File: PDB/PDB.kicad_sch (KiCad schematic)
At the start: 0 parts

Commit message: test
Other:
- added sheet 5V@12A (5v.kicad_sch)
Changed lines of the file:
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@@
 	(generator "eeschema")
 	(generator_version "9.0")
-	(paper "A4")
+	(paper "User" 424.18 177.8)
+	(sheet
+		(at 125.73 40.64)
+		(size 25.4 8.89)
+		(exclude_from_sim no)
+		(in_bom yes)
+		(on_board yes)
+		(dnp no)
+		(fields_autoplaced yes)
+		(stroke
+			(width 0.1524)
+			(type solid)
+		)
+		(fill
+			(color 0 0 0 0.0000)
+		)
+		(property "Sheetname" "5V@12A"
+			(at 125.73 39.9284 0)
+			(effects
+				(font
+					(size 1.27 1.27)
+				)
+				(justify left bottom)
+			)
+		)
+		(property "Sheetfile" "5v.kicad_sch"
+			(at 125.73 50.1146 0)
+			(effects
+				(font
+					(size 1.27 1.27)
+				)
+				(justify left top)
+			)
+		)
+		(instances
+			(project "PDB"
+				(path "/a9cf05c4-aac5-4cf1-b700-1d3045f8dfbd"
+					(page "2")
+				)
+			)
+		)
+	)
 	(sheet_instances
 		(path "/"

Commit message: did the microcontroller
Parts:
- added C10, C13: 2.2uF, Capacitor_SMD:C_1206_3216Metric, symbol Device:C
- added C11, C17, C19, C20, C21, C9: 100nF, Capacitor_SMD:C_1206_3216Metric, symbol Device:C
- added C8: 4.7uF, Capacitor_SMD:C_1206_3216Metric, symbol Device:C
- added D3, D4, D5, D6, D7: LED, LED_SMD:LED_0805_2012Metric, symbol Device:LED
- added R16, R27, R6, R8, R9: 270, Resistor_SMD:R_1206_3216Metric_Pad1.30x1.75mm_HandSolder, symbol Device:R
- added TP5, TP6: TestPoint, TestPoint:TestPoint_Pad_D2.5mm, symbol Connector:TestPoint
- added U2: STM32H742VGTx, Package_QFP:LQFP-100_14x14mm_P0.5mm, symbol MCU_ST_STM32H7:STM32H742VGTx
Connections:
- new net: R27.1, U2.52 (PB13)
- new net: D7.2 (A), R27.2
- new net: C13.2, U2.48 (VCAP)
- new net: R8.1, U2.45 (PE15)
- new net: D4.2 (A), R8.2
- new net: R16.1, U2.51 (PB12)
- new net: D6.2 (A), R16.2
- new net: R9.1, U2.44 (PE14)
- new net: D5.2 (A), R9.2
- new net: R6.1, U2.43 (PE13)
- new net: C10.2, U2.73 (VCAP)
- new net: D3.2 (A), R6.2
- new net +3.3V: C11.2, C17.1, C19.1, C20.1, C21.1, C8.1, C9.1, TP6.1, U2.100 (VDD), U2.11 (VDD), U2.20 (VREF+), U2.21 (VDDA), U2.27 (VDD), U2.50 (VDD), U2.75 (VDD)
- new net BOOT0: U2.94 (BOOT0)
- new net CS: U2.28 (PA4)
- new net D+: U2.71 (PA12)
- new net D-: U2.70 (PA11)
- new net GND: C10.1, C11.1, C13.1, C17.2, C19.2, C20.2, C21.2, C8.2, C9.2, D3.1 (K), D4.1 (K), D5.1 (K), D6.1 (K), D7.1 (K), TP5.1, U2.10 (VSS), U2.19 (VSSA), U2.26 (VSS), U2.49 (VSS), U2.74 (VSS), U2.99 (VSS)
- new net INT: U2.67 (PA8)
- new net MISO: U2.30 (PA6)
- new net MOSI: U2.31 (PA7)
- new net PA0: U2.22 (PA0)
- new net PA3: U2.25 (PA3)
- new net PB0: U2.34 (PB0)
- new net PB1: U2.35 (PB1)
- new net PB10: U2.46 (PB10)
- new net PB11: U2.47 (PB11)
- new net PB2: U2.36 (PB2)
- new net PC0: U2.15 (PC0)
- new net PC2: U2.17 (PC2_C)
- new net PC3: U2.18 (PC3_C)
- new net PC4: U2.32 (PC4)
- new net PC5: U2.33 (PC5)
- new net PE11: U2.41 (PE11)
- new net PE12: U2.42 (PE12)
- new net PE7: U2.37 (PE7)
- new net PE8: U2.38 (PE8)
- new net PE9: U2.39 (PE9)
- new net RST: U2.68 (PA9)
- new net SCK: U2.29 (PA5)
- new net SWCLK: U2.76 (PA14)
- new net SWDIO: U2.72 (PA13)
- new net SWO/TRACE: U2.89 (PB3)
- no-connect marks 0 -> 51
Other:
- note added: "TBD"

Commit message: Add 5V@4A
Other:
- added sheet 3V3@1A (3v3_1a.kicad_sch)
- added sheet 5V@4A (5v_4a.kicad_sch)
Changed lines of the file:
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@@
+		)
+	)
+	(sheet
+		(at 271.78 52.07)
+		(size 17.78 8.89)
+		(exclude_from_sim no)
+		(in_bom yes)
+		(on_board yes)
+		(dnp no)
+		(fields_autoplaced yes)
+		(stroke
+			(width 0.1524)
+			(type solid)
+		)
+		(fill
+			(color 0 0 0 0)
+		)
+		(property "Sheetname" "3V3@1A"
+			(at 271.78 51.3584 0)
+			(show_name no)
+			(do_not_autoplace no)
+			(effects
+				(font
+					(size 1.27 1.27)
+				)
+				(justify left bottom)
+			)
+		)
+		(property "Sheetfile" "3v3_1a.kicad_sch"
+			(at 271.78 61.5446 0)
+			(show_name no)
+			(do_not_autoplace no)
+			(effects
+				(font
+					(size 1.27 1.27)
+				)
+				(justify left top)
+			)
+		)
+		(instances
+			(project "PDB"
+				(path "/a9cf05c4-aac5-4cf1-b700-1d3045f8dfbd"
+					(page "4")
+				)
+			)
+		)
+	)
+	(sheet
+		(at 271.78 38.1)
+		(size 17.78 8.89)
+		(exclude_from_sim no)
+		(in_bom yes)
+		(on_board yes)
+		(dnp no)
+		(fields_autoplaced yes)
+		(stroke
+			(width 0.1524)
+			(type solid)
+		)
+		(fill
+			(color 0 0 0 0)
+		)
+		(property "Sheetname" "5V@4A"
+			(at 271.78 37.3884 0)
+			(show_name no)
+			(do_not_autoplace no)
+			(effects
+				(font
+					(size 1.27 1.27)
+				)
+				(justify left bottom)
+			)
+		)
+		(property "Sheetfile" "5v_4a.kicad_sch"
+			(at 271.78 47.5746 0)
+			(show_name no)
+			(do_not_autoplace no)
+			(effects
+				(font
+					(size 1.27 1.27)
+				)
+				(justify left top)
+			)
+		)
+		(instances
+			(project "PDB"
+				(path "/a9cf05c4-aac5-4cf1-b700-1d3045f8dfbd"
+					(page "3")
+				)
+			)
 		)
 	)

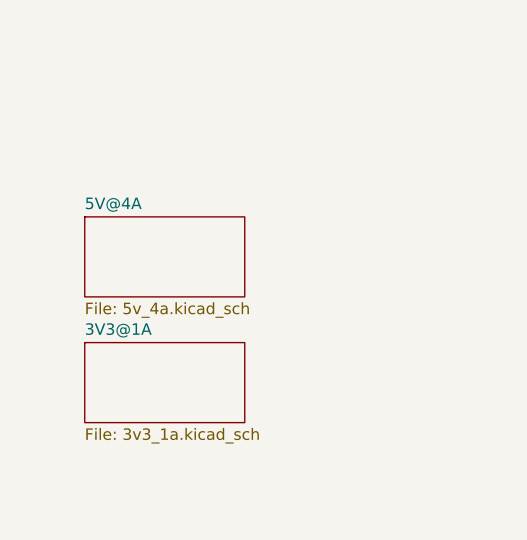
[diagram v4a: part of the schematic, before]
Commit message: Add 3v3@1a
unified the batery lables between sub schematics and changed Iout symbols for power pins to avoid layout issues for trying to match multiple bateries and Iouts without footprints
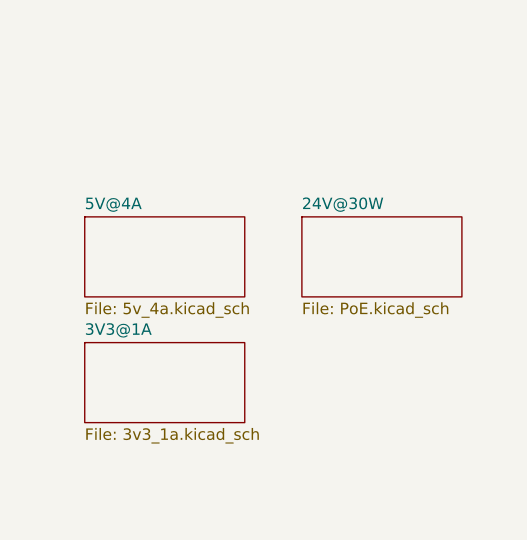
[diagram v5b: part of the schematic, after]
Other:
- added sheet 24V@30W (PoE.kicad_sch)
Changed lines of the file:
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@@
+	)
+	(sheet
+		(at 295.91 38.1)
+		(size 17.78 8.89)
+		(exclude_from_sim no)
+		(in_bom yes)
+		(on_board yes)
+		(dnp no)
+		(fields_autoplaced yes)
+		(stroke
+			(width 0.1524)
+			(type solid)
+		)
+		(fill
+			(color 0 0 0 0)
+		)
+		(property "Sheetname" "24V@30W"
+			(at 295.91 37.3884 0)
+			(show_name no)
+			(do_not_autoplace no)
+			(effects
+				(font
+					(size 1.27 1.27)
+				)
+				(justify left bottom)
+			)
+		)
+		(property "Sheetfile" "PoE.kicad_sch"
+			(at 295.91 47.5746 0)
+			(show_name no)
+			(do_not_autoplace no)
+			(effects
+				(font
+					(size 1.27 1.27)
+				)
+				(justify left top)
+			)
+		)
+		(instances
+			(project "PDB"
+				(path "/a9cf05c4-aac5-4cf1-b700-1d3045f8dfbd"
+					(page "5")
+				)
+			)
+		)
 	)
 	(sheet

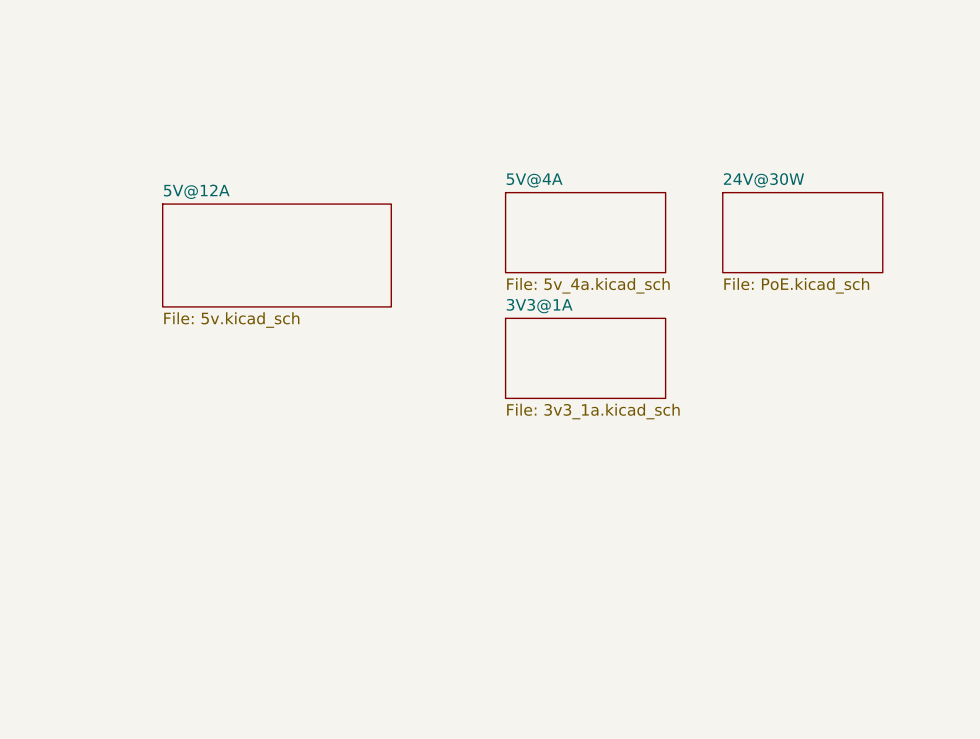
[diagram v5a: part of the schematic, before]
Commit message: Add 24V@1.5A
Filled 24V@1.5A schem and added hierarchal pins to each sub sheet
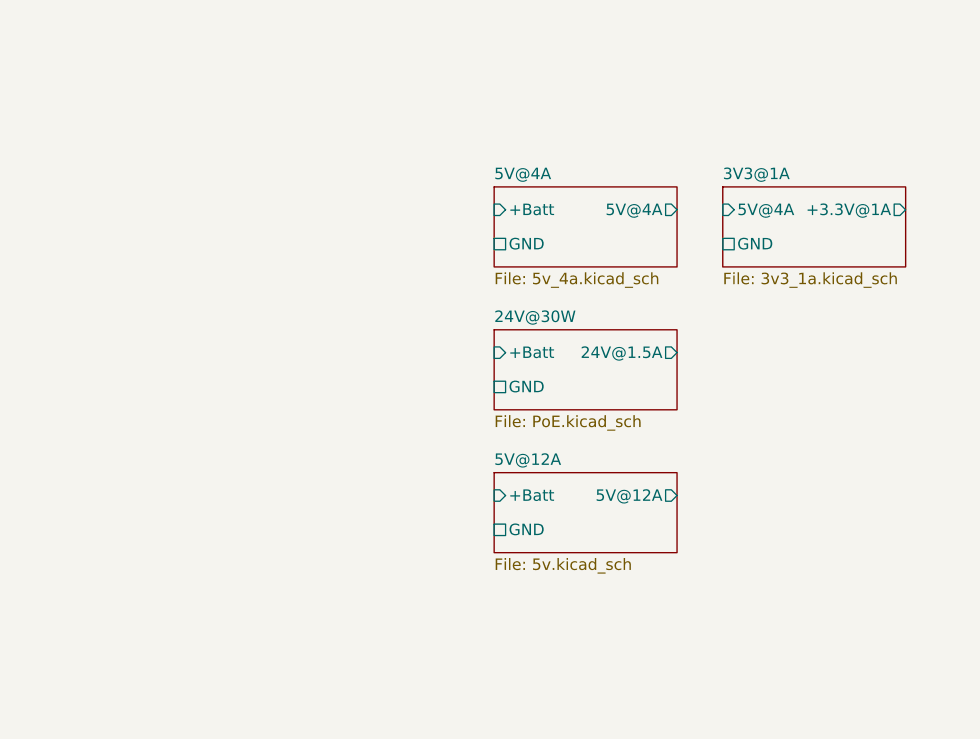
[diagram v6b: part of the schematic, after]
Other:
- sheet 24V@30W ports: added +Batt, 24V@1.5A, GND; removed none
- sheet 3V3@1A ports: added +3.3V@1A, 5V@4A, GND; removed none
- sheet 5V@12A ports: added +Batt, 5V@12A, GND; removed none
- sheet 5V@4A ports: added +Batt, 5V@4A, GND; removed none
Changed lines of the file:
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@@
 	)
 	(sheet
-		(at 295.91 38.1)
-		(size 17.78 8.89)
+		(at 270.51 53.34)
+		(size 20.32 8.89)
 		(exclude_from_sim no)
 		(in_bom yes)
@@
 		)
 		(property "Sheetname" "24V@30W"
-			(at 295.91 37.3884 0)
+			(at 270.51 52.6284 0)
 			(show_name no)
 			(do_not_autoplace no)
@@
 		)
 		(property "Sheetfile" "PoE.kicad_sch"
-			(at 295.91 47.5746 0)
-			(show_name no)
-			(do_not_autoplace no)
-			(effects
-				(font
-					(size 1.27 1.27)
-				)
-				(justify left top)
+			(at 270.51 62.8146 0)
+			(show_name no)
+			(do_not_autoplace no)
+			(effects
+				(font
+					(size 1.27 1.27)
+				)
+				(justify left top)
+			)
+		)
+		(pin "+Batt" input
+			(at 270.51 55.88 180)
+			(effects
+				(font
+					(size 1.27 1.27)
+				)
+				(justify left)
+			)
+		)
+		(pin "24V@1.5A" output
+			(at 290.83 55.88 0)
+			(effects
+				(font
+					(size 1.27 1.27)
+				)
+				(justify right)
+			)
+		)
+		(pin "GND" passive
+			(at 270.51 59.69 180)
+			(effects
+				(font
+					(size 1.27 1.27)
+				)
+				(justify left)
 			)
 		)
@@
 	)
 	(sheet
-		(at 233.68 39.37)
-		(size 25.4 11.43)
+		(at 270.51 69.215)
+		(size 20.32 8.89)
 		(exclude_from_sim no)
 		(in_bom yes)
@@
 		)
 		(property "Sheetname" "5V@12A"
-			(at 233.68 38.6584 0)
+			(at 270.51 68.5034 0)
 			(show_name no)
 			(do_not_autoplace no)
@@
 		)
 		(property "Sheetfile" "5v.kicad_sch"
-			(at 233.68 51.3846 0)
-			(show_name no)
-			(do_not_autoplace no)
-			(effects
-				(font
-					(size 1.27 1.27)
-				)
-				(justify left top)
+			(at 270.51 78.6896 0)
+			(show_name no)
+			(do_not_autoplace no)
+			(effects
+				(font
+					(size 1.27 1.27)
+				)
+				(justify left top)
+			)
+		)
+		(pin "+Batt" input
+			(at 270.51 71.755 180)
+			(effects
+				(font
+					(size 1.27 1.27)
+				)
+				(justify left)
+			)
+		)
+		(pin "5V@12A" output
+			(at 290.83 71.755 0)
+			(effects
+				(font
+					(size 1.27 1.27)
+				)
+				(justify right)
+			)
+		)
+		(pin "GND" passive
+			(at 270.51 75.565 180)
+			(effects
+				(font
+					(size 1.27 1.27)
+				)
+				(justify left)
 			)
 		)
@@
 	)
 	(sheet
-		(at 271.78 52.07)
-		(size 17.78 8.89)
+		(at 295.91 37.465)
+		(size 20.32 8.89)
 		(exclude_from_sim no)
 		(in_bom yes)
@@
 		)
 		(property "Sheetname" "3V3@1A"
-			(at 271.78 51.3584 0)
+			(at 295.91 36.7534 0)
 			(show_name no)
 			(do_not_autoplace no)
@@
 		)
 		(property "Sheetfile" "3v3_1a.kicad_sch"
-			(at 271.78 61.5446 0)
-			(show_name no)
-			(do_not_autoplace no)
-			(effects
-				(font
-					(size 1.27 1.27)
-				)
-				(justify left top)
+			(at 295.91 46.9396 0)
+			(show_name no)
+			(do_not_autoplace no)
+			(effects
+				(font
+					(size 1.27 1.27)
+				)
+				(justify left top)
+			)
+		)
+		(pin "+3.3V@1A" output
+			(at 316.23 40.005 0)
+			(effects
+				(font
+					(size 1.27 1.27)
+				)
+				(justify right)
+			)
+		)
+		(pin "5V@4A" input
+			(at 295.91 40.005 180)
+			(effects
+				(font
+					(size 1.27 1.27)
+				)
+				(justify left)
+			)
+		)
+		(pin "GND" passive
+			(at 295.91 43.815 180)
+			(effects
+				(font
+					(size 1.27 1.27)
+				)
+				(justify left)
 			)
 		)
@@
 	)
 	(sheet
-		(at 271.78 38.1)
-		(size 17.78 8.89)
+		(at 270.51 37.465)
+		(size 20.32 8.89)
 		(exclude_from_sim no)
 		(in_bom yes)
@@
 		)
 		(property "Sheetname" "5V@4A"
-			(at 271.78 37.3884 0)
+			(at 270.51 36.7534 0)
 			(show_name no)
 			(do_not_autoplace no)
@@
 		)
 		(property "Sheetfile" "5v_4a.kicad_sch"
-			(at 271.78 47.5746 0)
-			(show_name no)
-			(do_not_autoplace no)
-			(effects
-				(font
-					(size 1.27 1.27)
-				)
-				(justify left top)
-			)
-		)
+			(at 270.51 46.9396 0)
+			(show_name no)
+			(do_not_autoplace no)
+			(effects
+				(font
+					(size 1.27 1.27)
+				)
+				(justify left top)
+			)
+		)
+		(pin "+Batt" input
+			(at 270.51 40.005 180)
+			(effects
+				(font
+					(size 1.27 1.27)
+				)
+				(justify left)
+			)
+		)
+		(pin "5V@4A" output
+			(at 290.83 40.005 0)
+			(effects
+				(font
+					(size 1.27 1.27)
+				)
+				(justify right)
+			)
+		)
+		(pin "GND" passive
+			(at 270.51 43.815 180)
+			(effects
+				(font
+					(size 1.27 1.27)
+				)
+				(justify left)
+			)
+		)

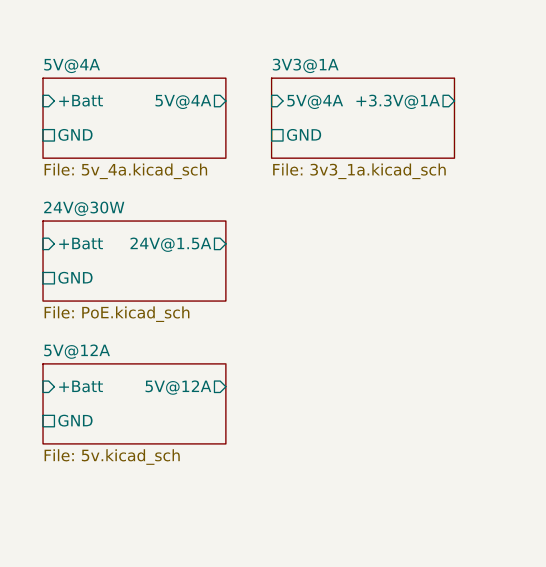
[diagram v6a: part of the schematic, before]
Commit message: finished USBC
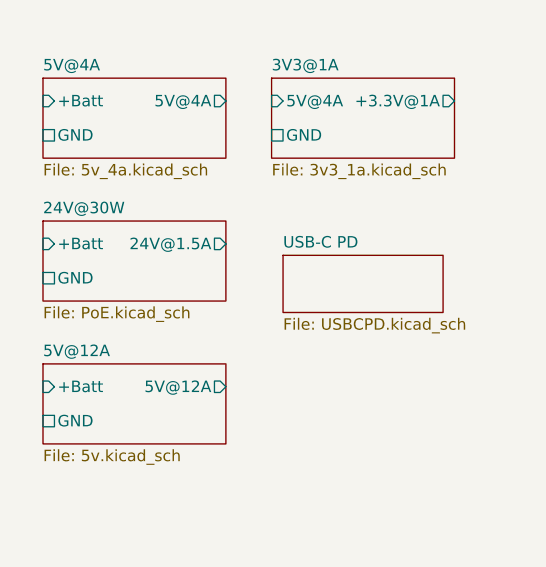
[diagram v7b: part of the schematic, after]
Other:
- added sheet USB-C PD (USBCPD.kicad_sch)
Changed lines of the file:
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@@
+	)
+	(sheet
+		(at 297.18 57.15)
+		(size 17.78 6.35)
+		(exclude_from_sim no)
+		(in_bom yes)
+		(on_board yes)
+		(dnp no)
+		(fields_autoplaced yes)
+		(stroke
+			(width 0.1524)
+			(type solid)
+		)
+		(fill
+			(color 0 0 0 0)
+		)
+		(property "Sheetname" "USB-C PD"
+			(at 297.18 56.4384 0)
+			(show_name no)
+			(do_not_autoplace no)
+			(effects
+				(font
+					(size 1.27 1.27)
+				)
+				(justify left bottom)
+			)
+		)
+		(property "Sheetfile" "USBCPD.kicad_sch"
+			(at 297.18 64.0846 0)
+			(show_name no)
+			(do_not_autoplace no)
+			(effects
+				(font
+					(size 1.27 1.27)
+				)
+				(justify left top)
+			)
+		)
+		(instances
+			(project "PDB"
+				(path "/a9cf05c4-aac5-4cf1-b700-1d3045f8dfbd"
+					(page "6")
+				)
+			)
+		)
 	)
 	(sheet
